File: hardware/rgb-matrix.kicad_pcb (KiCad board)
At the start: 4 copper layers, 58 x 58 mm, 138 parts, among them CON1 VEXT, P1 MATRIX_BOT, P10 PSOUTH, P11 PEAST, P12 WEST, P13 NORTH, P14 SOUTH, P15 EAST, P2 MATRIX_TOP, P3 SWD, P4 SPI3, P5 UART5, P6 VEXT, P7 USB_B, P8 PWEST, P9 PNORTH, SW1 RESET, SW2 BOOT, U1 74AC244, U2 74AC244, U3 74AC244, U4 ULN2803A, U5 STM32F405R, U6 LD3985M33R, U7 USBUF01W6, X1 8MHz

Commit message: Update component versions (ULN2308A and USB_B)
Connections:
- P7 pad 2: Net-(P7-Pad2) -> (no net)
- P7 pad 4: (no net) -> Net-(P7-Pad4)
- U7 pad 4: Net-(P7-Pad2) -> Net-(P7-Pad4)
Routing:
- net Net-(P7-Pad4): track 0.00 -> 7.74 mm
- net Net-(P7-Pad2): track 7.74 -> 0.00 mm

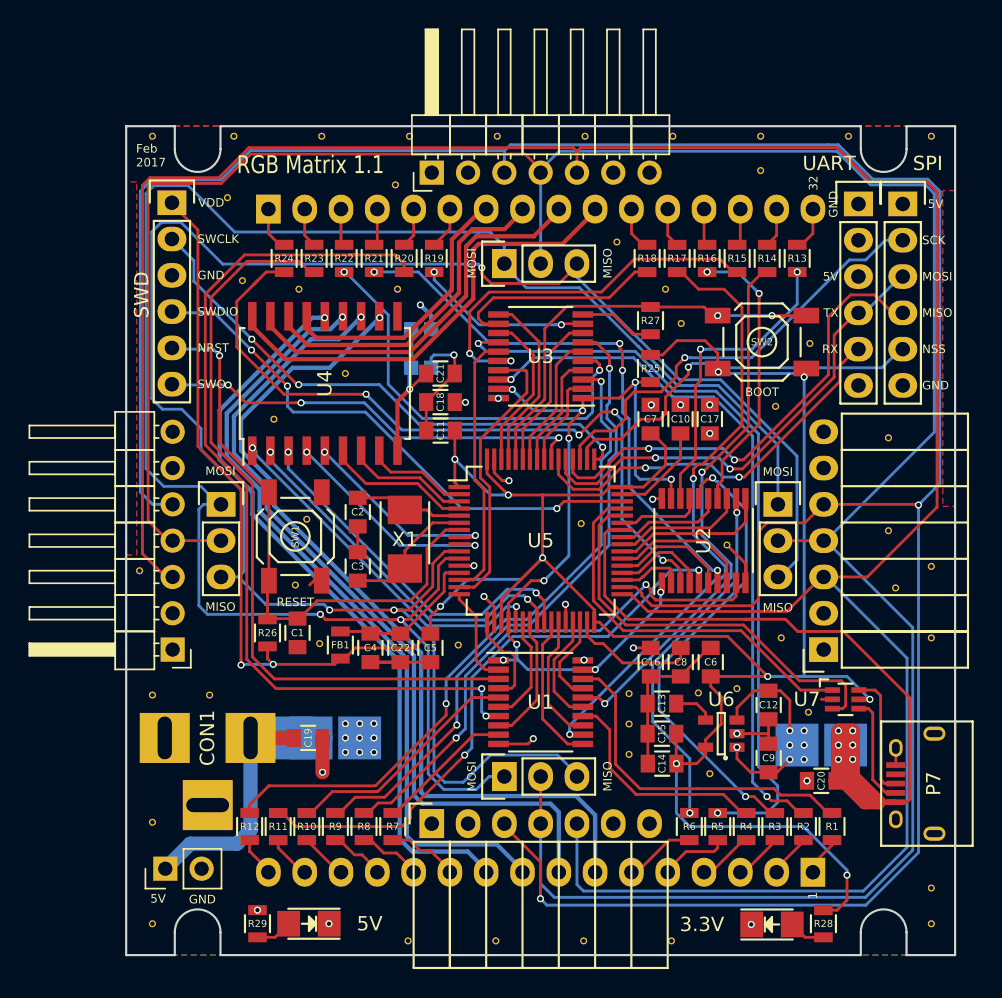
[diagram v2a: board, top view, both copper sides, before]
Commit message: PCB fixes for 1.1
* Disconnect DATA lines in daisy chain
* Fix barrel jack footprint (hole size)
* Fix some 3D models
* Update PCB netlist
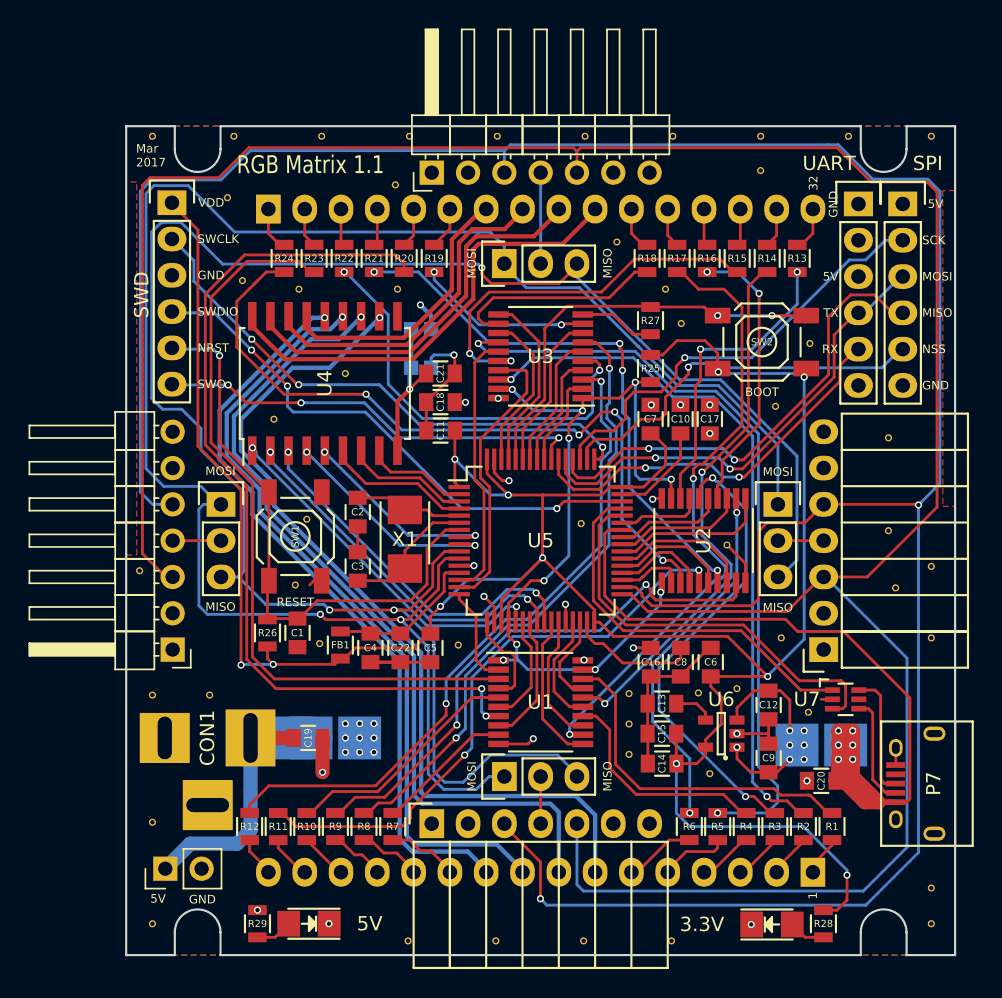
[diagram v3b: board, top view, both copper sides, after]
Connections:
- P10 pad 4: /daisy/DATA -> /daisy/DATASOUTH
- P11 pad 4: /daisy/DATA -> /daisy/DATAEAST
- P12 pad 2: /daisy/DATA -> /daisy/DATAWEST
- P13 pad 2: /daisy/DATA -> /daisy/DATANORTH
- P14 pad 2: /daisy/DATA -> /daisy/DATASOUTH
- P15 pad 2: /daisy/DATA -> /daisy/DATAEAST
- P7 pad 2: (no net) -> Net-(P7-Pad2)
- P7 pad 4: Net-(P7-Pad4) -> (no net)
- P8 pad 4: /daisy/DATA -> /daisy/DATAWEST
- P9 pad 4: /daisy/DATA -> /daisy/DATANORTH
- U7 pad 4: Net-(P7-Pad4) -> Net-(P7-Pad2)
- U7 pad 5: +3V3 -> (no net)
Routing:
- net /daisy/DATA: track 184.3 -> 0.00 mm
- net +3V3: track 198.4 -> 190.6 mm, vias 12 -> 11
- net Net-(P7-Pad4): track 7.74 -> 0.00 mm
- net Net-(P7-Pad2): track 0.00 -> 7.74 mm
- net /daisy/DATANORTH: track 0.00 -> 6.86 mm
- net /daisy/DATAEAST: track 0.00 -> 3.70 mm
- net /daisy/DATASOUTH: track 0.00 -> 3.45 mm
- net /daisy/DATAWEST: track 0.00 -> 3.35 mm
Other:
- board text added: "Mar 2017"
- board text removed: "Feb 2017"
